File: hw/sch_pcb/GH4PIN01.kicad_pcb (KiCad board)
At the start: 2 copper layers, 19.8 x 40.1 mm, 11 parts, among them J1 SM04B-GHS-TB, J2 SM04B-GHS-TB, J3 HEADER_2x05_PARALLEL, J4 SM04B-GHS-TB, J5 SM04B-GHS-TB, M1 HOLE M3, M2 HOLE M3, M3 HOLE, M4 HOLE

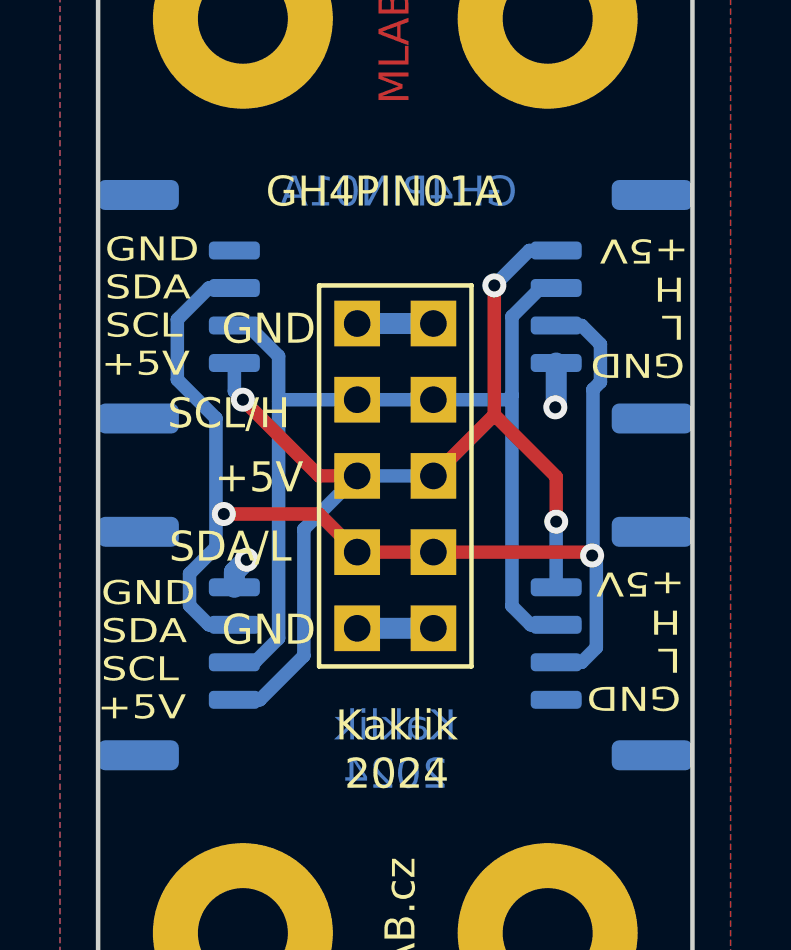
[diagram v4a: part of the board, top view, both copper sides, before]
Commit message: Move the connectors more inside to PCB.
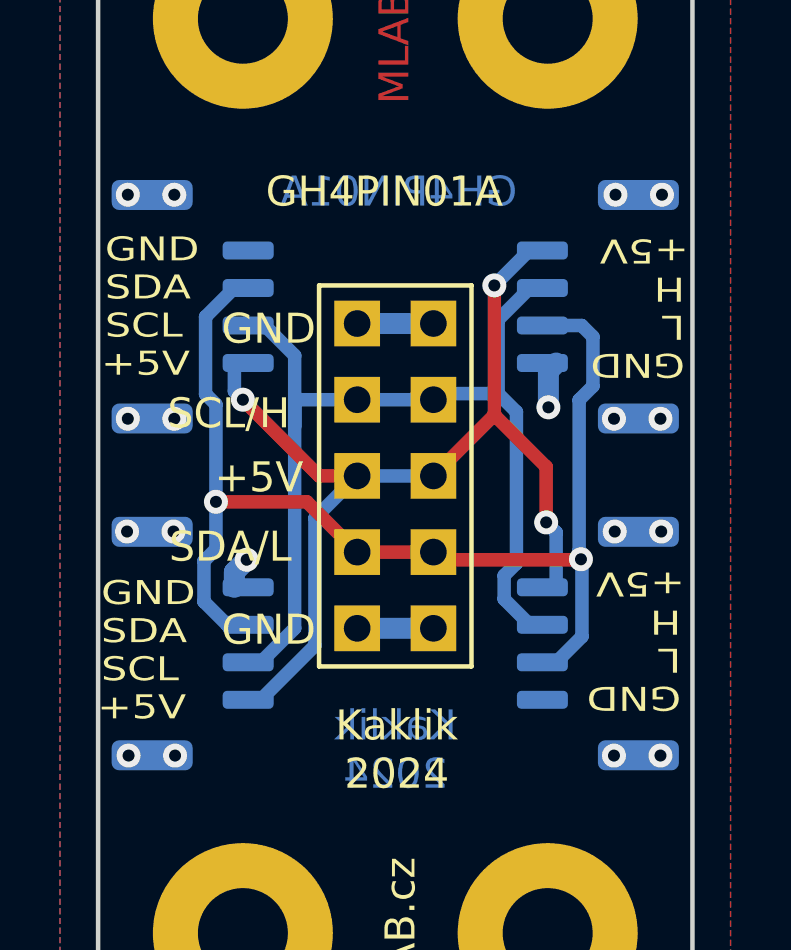
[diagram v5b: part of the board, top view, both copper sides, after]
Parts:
- moved J4 0.46 mm to (141.7, 99.4)
- moved J5 0.46 mm to (141.7, 110.6)
- moved J1 0.46 mm to (155.3, 110.6)
- moved J2 0.46 mm to (155.3, 99.4)
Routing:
- net /SDA/CAN_L: track 40.9 -> 38.3 mm
- net /SCL/CAN_H: track 34.2 -> 35.9 mm
- net GND: track 7.66 -> 8.52 mm, vias 2 -> 18
